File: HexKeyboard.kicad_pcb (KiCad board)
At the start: 2 copper layers, 132.2 x 144.1 mm, 82 parts, among them J1 Micro_SD_Card, J2 Conn_01x04, J3 Conn_02x04_Odd_Even, J5 USB_A, SW1 SW_1, SW10 SW_10, SW11 SW_11, SW12 SW_12, SW13 SW_13, SW14 SW_14, SW15 SW_15, SW16 SW_16, SW17 SW_17, SW18 SW_18, SW19 SW_19, SW2 SW_2, SW20 SW_20, SW21 SW_21, SW22 SW_22, SW23 SW_23, SW24 SW_24, SW25 SW_25, SW3 SW_3, SW4 SW_4, SW5 SW_5, SW6 SW_6, SW7 SW_7, SW8 SW_8, SW9 SW_9, U1 AMS1117-3.3, U2 74LVC125, U3 ATmega32U4-AU, U4 AT24CS64-XHM, U5 MAX7219, Y1 16MHz

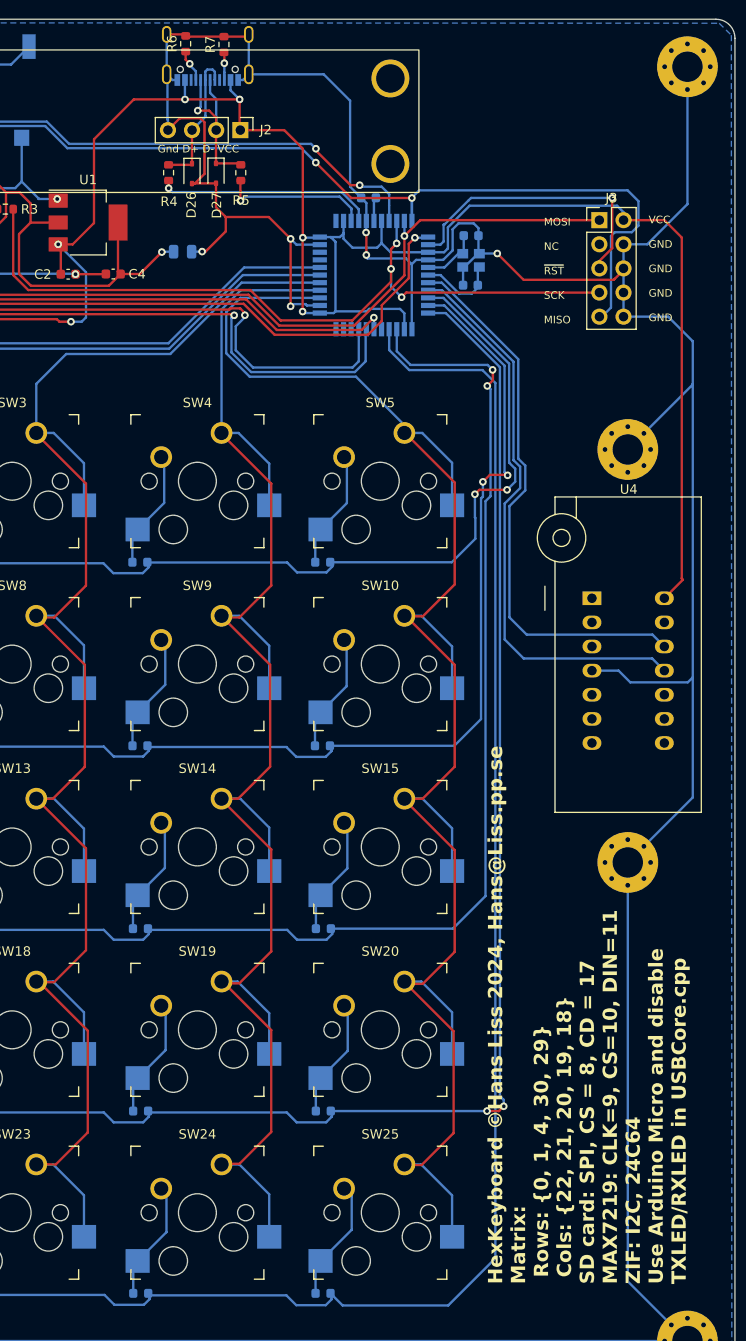
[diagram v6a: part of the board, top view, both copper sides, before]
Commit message: Added serial port. Added new pin numbers to sketch
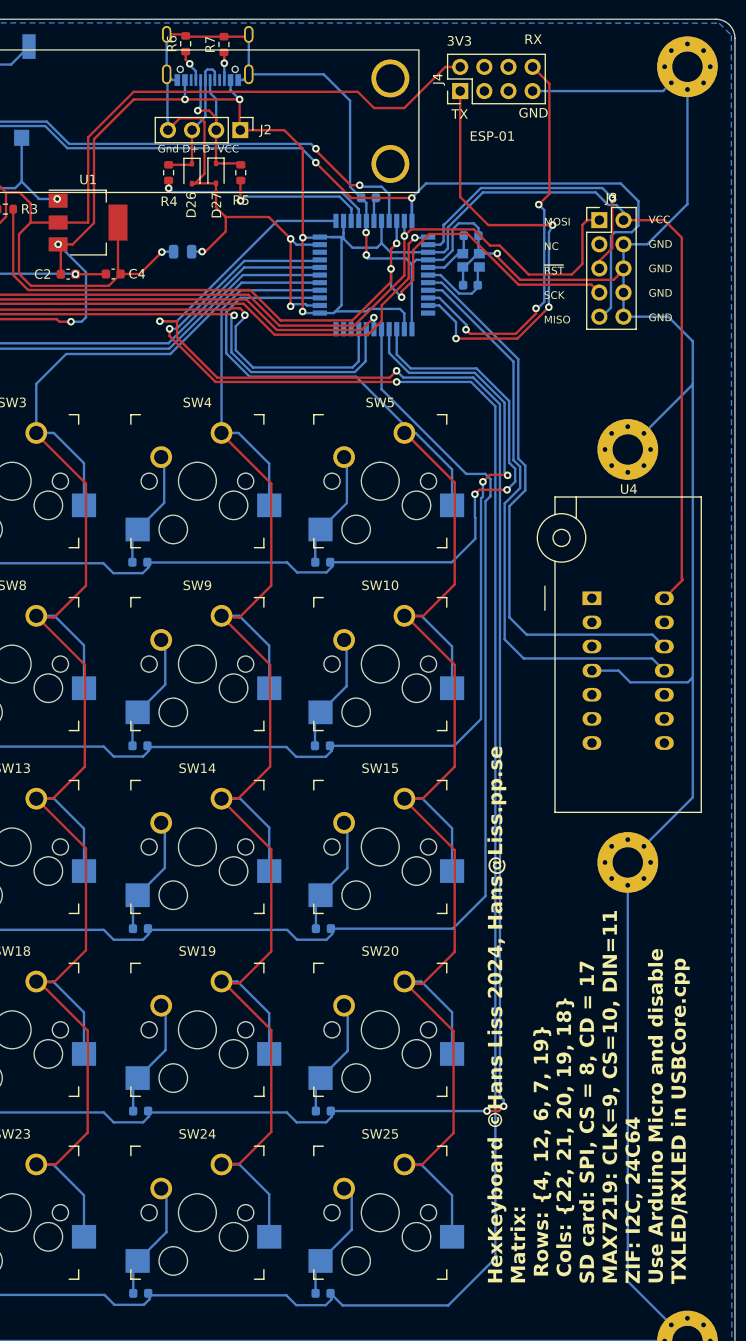
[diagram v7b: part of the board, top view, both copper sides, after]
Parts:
- added J4: Conn_02x04_Odd_Even, Connector_PinHeader_2.54mm:PinHeader_2x04_P2.54mm_Vertical, F.Cu at (135.2, 45.8)
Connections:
- U3 pad 1: unconnected-(U3-PE6-Pad1) -> ROW3
- U3 pad 20: ROW0 -> /RX
- U3 pad 21: ROW1 -> /TX
- U3 pad 22: ROW3 -> unconnected-(U3-PD5-Pad22)
- U3 pad 25: ROW2 -> ROW0
- U3 pad 26: ROW4 -> ROW1
- U3 pad 27: unconnected-(U3-PD7-Pad27) -> ROW2
- U3 pad 41: unconnected-(U3-PF0-Pad41) -> ROW4
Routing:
- net +3.3V: track 64.1 -> 119.8 mm
- net ROW3: track 188.0 -> 238.1 mm, vias 2 -> 4
- net /TX: track 0.00 -> 47.4 mm, vias 0 -> 3
- net /RX: track 0.00 -> 42.1 mm, vias 0 -> 3
- net ROW4: track 208.5 -> 248.2 mm, vias 0 -> 2
- net GND: track 708.8 -> 726.4 mm
- net /SCK: track 81.5 -> 88.8 mm
- net /MOSI: track 95.0 -> 101.4 mm
- net ROW2: track 168.6 -> 165.2 mm, vias 2 -> 0
- net VCC: track 249.2 -> 251.5 mm
- net ROW1: track 149.1 -> 151.3 mm
- net ROW0: track 131.5 -> 132.7 mm
- net /~{RESET}: track 30.4 -> 31.3 mm
- net /MISO: track 102.2 -> 102.8 mm
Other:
- board text added: "3V3"
- board text added: "ESP-01"
- board text added: "GND"
- board text added: "HexKeyboard ©Hans Liss 2024, Hans@Liss.pp.se Matrix: Rows: {4, 12, 6, 7, 19} Cols: {22, 21, 20, 19, 18} SD card: SPI, CS = 8, CD = 17 MAX7219: CLK=9, CS=10, DIN=11 ZIF: I2C, 24C64 Use Arduino Micro and disable TXLED/RXLED in USBCore.cpp"
- board text added: "RX"
- board text added: "TX"
- board text removed: "HexKeyboard ©Hans Liss 2024, Hans@Liss.pp.se Matrix: Rows: {0, 1, 4, 30, 29} Cols: {22, 21, 20, 19, 18} SD card: SPI, CS = 8, CD = 17 MAX7219: CLK=9, CS=10, DIN=11 ZIF: I2C, 24C64 Use Arduino Micro and disable TXLED/RXLED in USBCore.cpp"

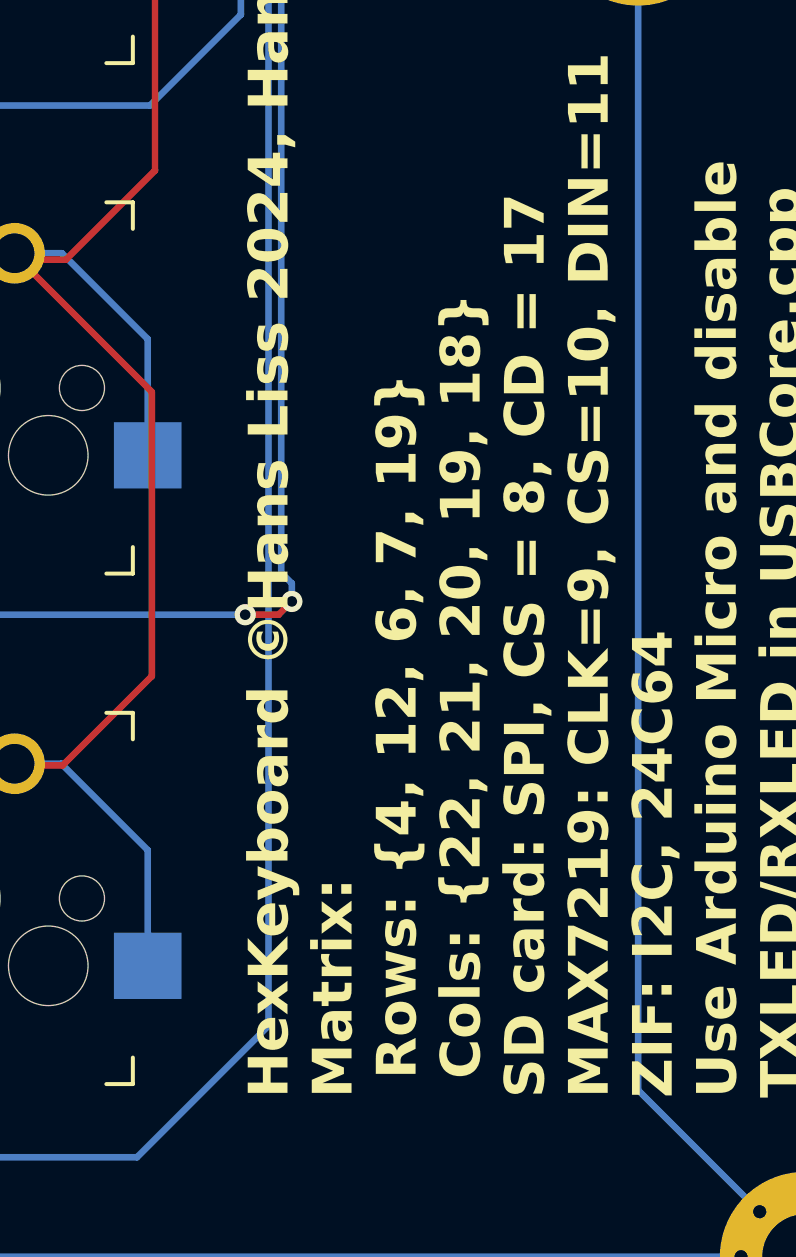
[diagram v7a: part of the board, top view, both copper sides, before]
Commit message: Fixed some erroneous pin numbers
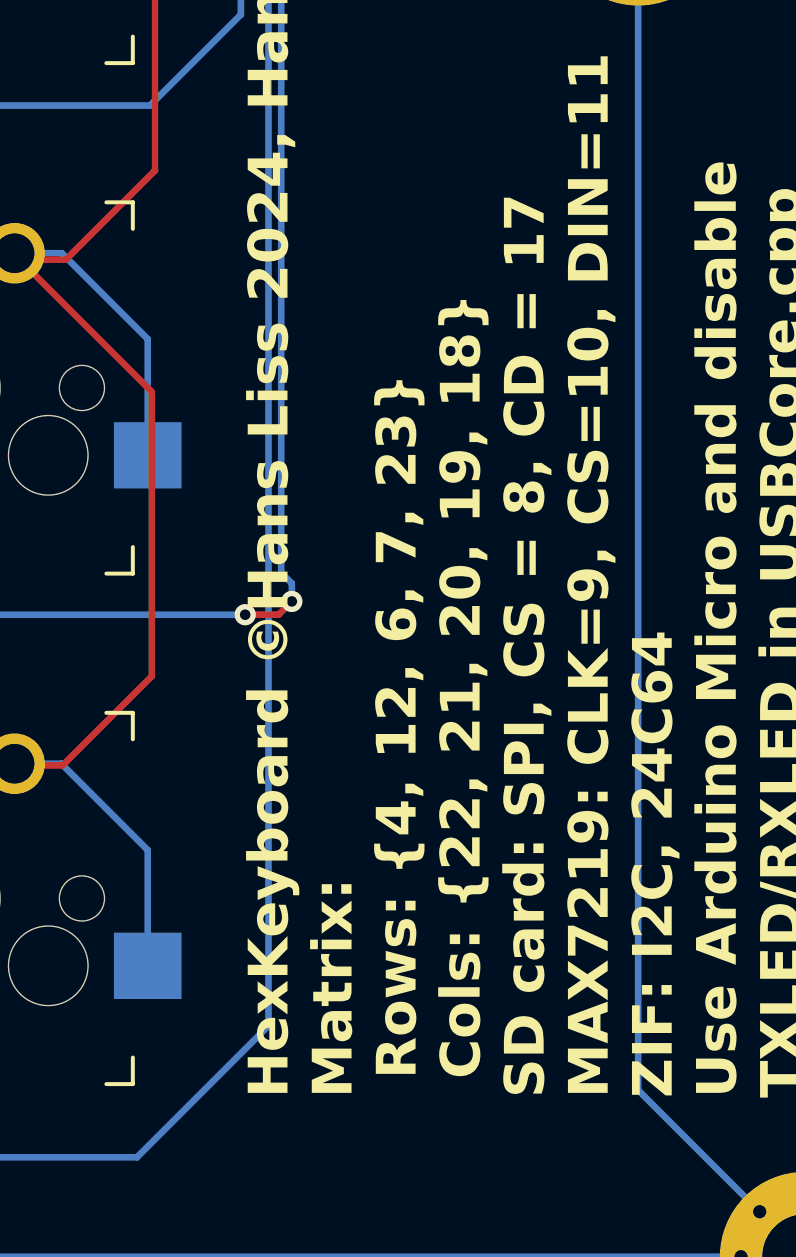
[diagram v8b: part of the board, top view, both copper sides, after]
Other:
- board text added: "HexKeyboard ©Hans Liss 2024, Hans@Liss.pp.se Matrix: Rows: {4, 12, 6, 7, 23} Cols: {22, 21, 20, 19, 18} SD card: SPI, CS = 8, CD = 17 MAX7219: CLK=9, CS=10, DIN=11 ZIF: I2C, 24C64 Use Arduino Micro and disable TXLED/RXLED in USBCore.cpp"
- board text removed: "HexKeyboard ©Hans Liss 2024, Hans@Liss.pp.se Matrix: Rows: {4, 12, 6, 7, 19} Cols: {22, 21, 20, 19, 18} SD card: SPI, CS = 8, CD = 17 MAX7219: CLK=9, CS=10, DIN=11 ZIF: I2C, 24C64 Use Arduino Micro and disable TXLED/RXLED in USBCore.cpp"
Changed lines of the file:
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@@
     (effects (font (size 1 1) (thickness 0.15)) (justify left bottom))
   )
-  (gr_text "HexKeyboard ©Hans Liss 2024, Hans@Liss.pp.se\nMatrix:\n Rows: {4, 12, 6, 7, 19}\n Cols: {22, 21, 20, 19, 18}\nSD card: SPI, CS = 8, CD = 17\nMAX7219: CLK=9, CS=10, DIN=11\nZIF: I2C, 24C64\nUse Arduino Micro and disable\nTXLED/RXLED in USBCore.cpp" (at 159.1 171.35 90) (layer "F.SilkS")
+  (gr_text "HexKeyboard ©Hans Liss 2024, Hans@Liss.pp.se\nMatrix:\n Rows: {4, 12, 6, 7, 23}\n Cols: {22, 21, 20, 19, 18}\nSD card: SPI, CS = 8, CD = 17\nMAX7219: CLK=9, CS=10, DIN=11\nZIF: I2C, 24C64\nUse Arduino Micro and disable\nTXLED/RXLED in USBCore.cpp" (at 159.1 171.35 90) (layer "F.SilkS")
     (effects (font (size 1.5 1.5) (thickness 0.3) bold) (justify left bottom))
   )
